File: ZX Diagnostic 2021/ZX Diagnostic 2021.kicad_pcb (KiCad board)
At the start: 2 copper layers, 57.9 x 61.6 mm, 30 parts, among them J1 Cartridge, M1 Mounting, M2 Mounting, M3 Mounting, M4 Mounting, U1 27C512, U2 74HCT373

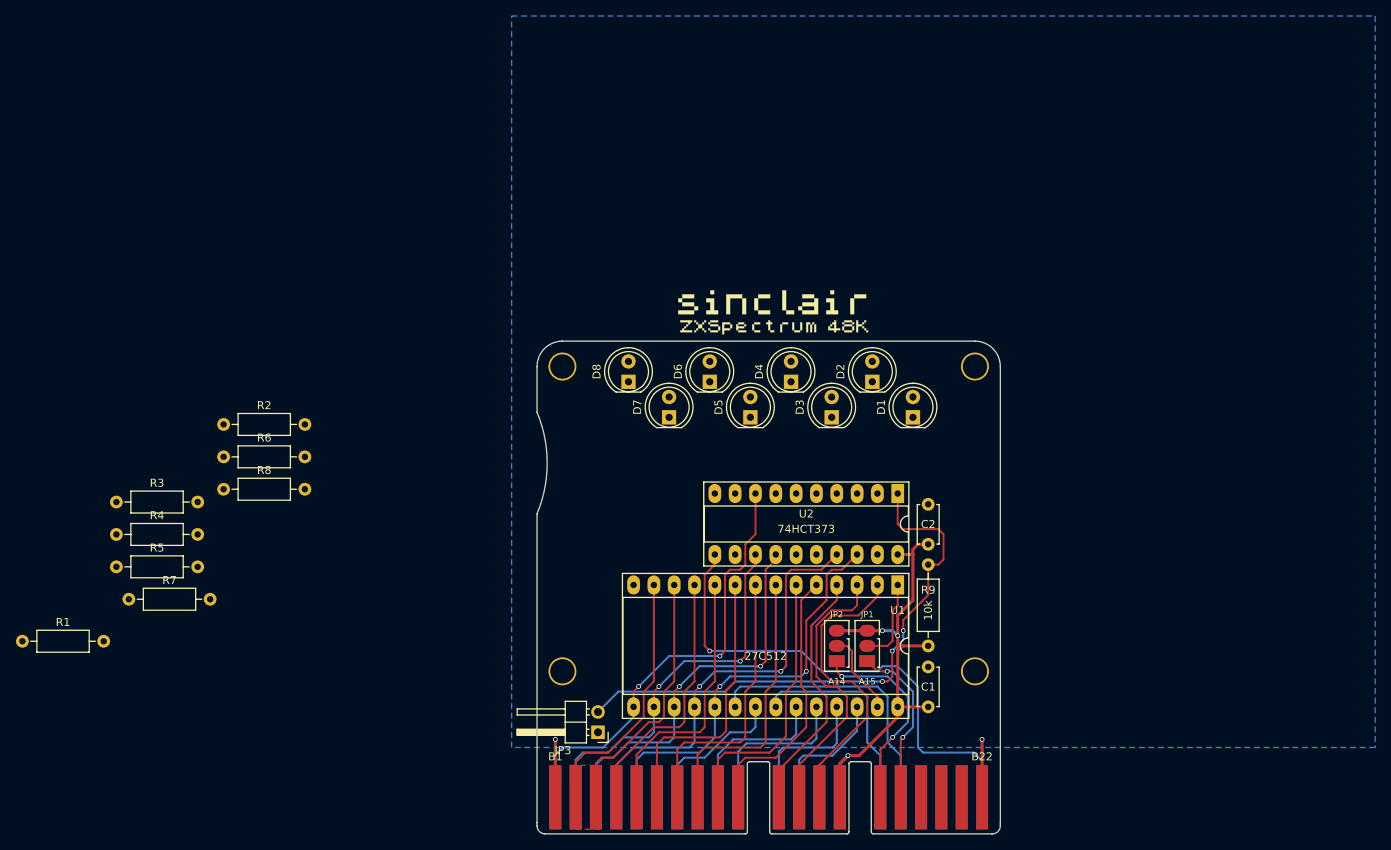
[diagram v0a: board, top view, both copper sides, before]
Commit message: Diagnostic layout done
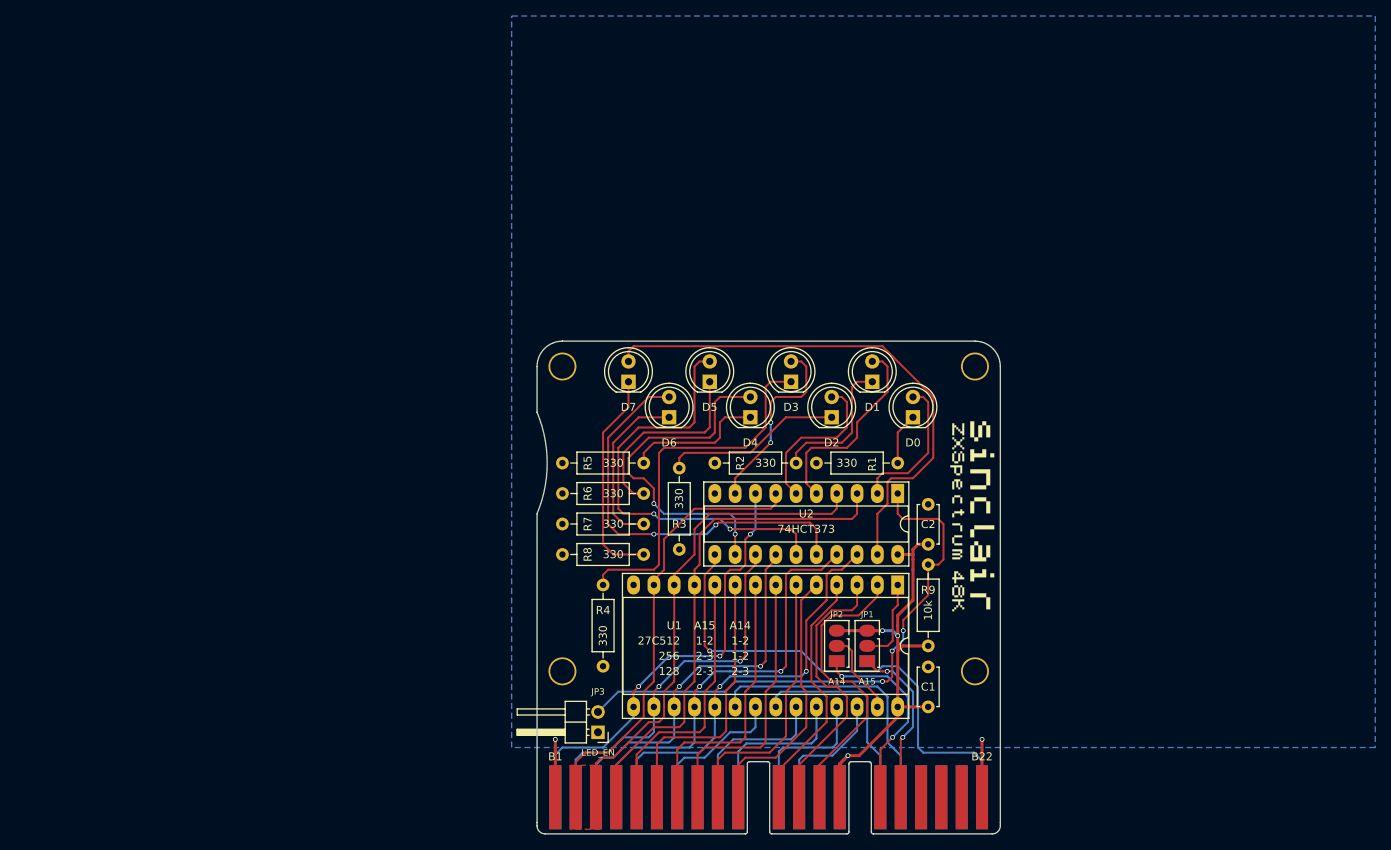
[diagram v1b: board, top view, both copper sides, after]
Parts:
- added sinclair_title: , artwork:sinclair_title, B.Cu at (177.5, 93.3)
- moved R1 111.7 mm to (165.4, 74.3), turned to 180 degrees
- moved R2 71.7 mm to (152.7, 74.3), turned to 180 degrees
- moved R3 70.5 mm to (138.0, 74.9), turned to 270 degrees
- moved R5 67.2 mm to (133.6, 74.3), turned to 180 degrees
- moved R7 65.0 mm to (133.6, 81.9), turned to 180 degrees
- moved R4 61.2 mm to (128.5, 89.5), turned to 270 degrees
- moved R8 53.1 mm to (133.6, 85.7), turned to 180 degrees
- moved R6 52.7 mm to (133.6, 78.1), turned to 180 degrees
- moved sinclair_title 43.0 mm to (177.4, 68.6), turned to 270 degrees
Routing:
- net Net-(D8-Pad2): track 0.00 -> 66.4 mm
- net Net-(D6-Pad2): track 0.00 -> 53.7 mm, vias 0 -> 2
- net Net-(D7-Pad2): track 0.00 -> 51.2 mm, vias 0 -> 2
- net Net-(D4-Pad1): track 0.00 -> 45.9 mm
- net Net-(D5-Pad2): track 0.00 -> 43.8 mm, vias 0 -> 2
- net /D0: track 32.5 -> 62.3 mm
- net /D1: track 32.2 -> 61.0 mm
- net Net-(D8-Pad1): track 0.00 -> 27.2 mm
- net Net-(D2-Pad2): track 0.00 -> 25.4 mm
- net Net-(D6-Pad1): track 0.00 -> 24.7 mm
- net Net-(D4-Pad2): track 0.00 -> 23.6 mm, vias 0 -> 2
- net /D2: track 32.3 -> 55.6 mm
- net Net-(D3-Pad1): track 0.00 -> 23.1 mm
- net Net-(D7-Pad1): track 0.00 -> 21.5 mm
- net Net-(D3-Pad2): track 0.00 -> 19.9 mm
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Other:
- board text added: "1-2"
- board text added: "128"
- board text added: "2-3"
- board text added: "256"
- board text added: "A14"
- board text added: "A15"
- board text added: "D0"
- board text added: "D1"
- board text added: "D2"
- board text added: "D3"
- board text added: "D4"
- board text added: "D5"
- board text added: "D6"
- board text added: "D7"
- board text added: "ZX Diagnostic 2.021 github.com/tebl"
- board text removed: "ZX Cartridge 2.021 github.com/tebl"
